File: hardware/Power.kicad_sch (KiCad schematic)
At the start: 70 parts, among them J10 I2C, J3 ESTOP, J4 PWR, J5 Conn_ARM_JTAG_SWD_10, J7 FAN, J9 DEBUG, Q1 MMBT5401LT1G, Q2 PSMN4R8-100BSEJ, Q3 MMBT3904, Q5 PSMN4R8-100BSEJ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

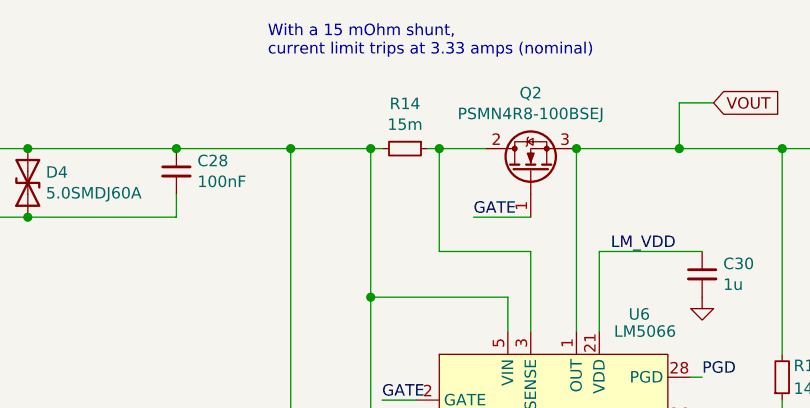
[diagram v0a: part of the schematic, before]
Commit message: Rsns to 5m (13A limit)
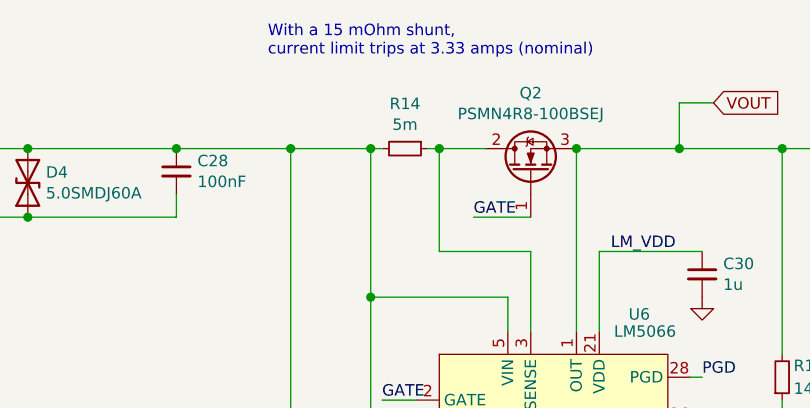
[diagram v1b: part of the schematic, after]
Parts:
- R14: value 15m -> 5m; D1PN WSLH-.015CT-ND -> 696-1182-2-ND; MFN Vishay Dale -> Riedon; MPN WSL2512R0150FEA18 -> CSR2512B0R005F
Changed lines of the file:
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@@
   (junction (at 259.08 97.79) (diameter 1.016) (color 0 0 0 0))
   (junction (at 259.08 105.41) (diameter 1.016) (color 0 0 0 0))
+  (no_connect (at 120.65 78.74))
+  (no_connect (at 120.65 81.28))
+  (no_connect (at 177.8 45.72))
+  (no_connect (at 198.12 55.88))
+  (no_connect (at 177.8 55.88))
   (no_connect (at 120.65 76.2))
-  (no_connect (at 177.8 55.88))
   (no_connect (at 254 50.8))
-  (no_connect (at 120.65 81.28))
-  (no_connect (at 90.17 83.82))
-  (no_connect (at 177.8 45.72))
   (no_connect (at 120.65 73.66))
   (no_connect (at 255.27 100.33))
-  (no_connect (at 198.12 55.88))
-  (no_connect (at 120.65 78.74))
+  (no_connect (at 90.17 83.82))
   (wire (pts (xy 16.51 120.65) (xy 25.4 120.65))
     (stroke (width 0) (type solid) (color 0 0 0 0))
@@
     (in_bom yes) (on_board yes)
     (property "Reference" "R14" (id 0) (at 88.9 22.9616 90))
-    (property "Value" "15m" (id 1) (at 88.9 25.273 90))
+    (property "Value" "5m" (id 1) (at 88.9 25.273 90))
     (property "Footprint" "Resistor_SMD:R_2512_6332Metric" (id 2) (at 88.9 27.94 0)
       (effects (font (size 1.27 1.27)) hide)
@@
       (effects (font (size 1.27 1.27)) hide)
     )
-    (property "D1PN" "WSLH-.015CT-ND" (id 5) (at 88.9 27.94 90)
-      (effects (font (size 1.27 1.27)) hide)
-    )
-    (property "MFN" "Vishay Dale" (id 6) (at 88.9 27.94 90)
-      (effects (font (size 1.27 1.27)) hide)
-    )
-    (property "MPN" "WSL2512R0150FEA18" (id 7) (at 88.9 27.94 90)
-      (effects (font (size 1.27 1.27)) hide)
-    )
+    (property "D1PN" "696-1182-2-ND" (id 5) (at 88.9 27.94 90)
+      (effects (font (size 1.27 1.27)) hide)
+    )
+    (property "MFN" "Riedon" (id 6) (at 88.9 27.94 90)
+      (effects (font (size 1.27 1.27)) hide)
+    )
+    (property "MPN" "CSR2512B0R005F" (id 7) (at 88.9 27.94 90)
+      (effects (font (size 1.27 1.27)) hide)
+    )

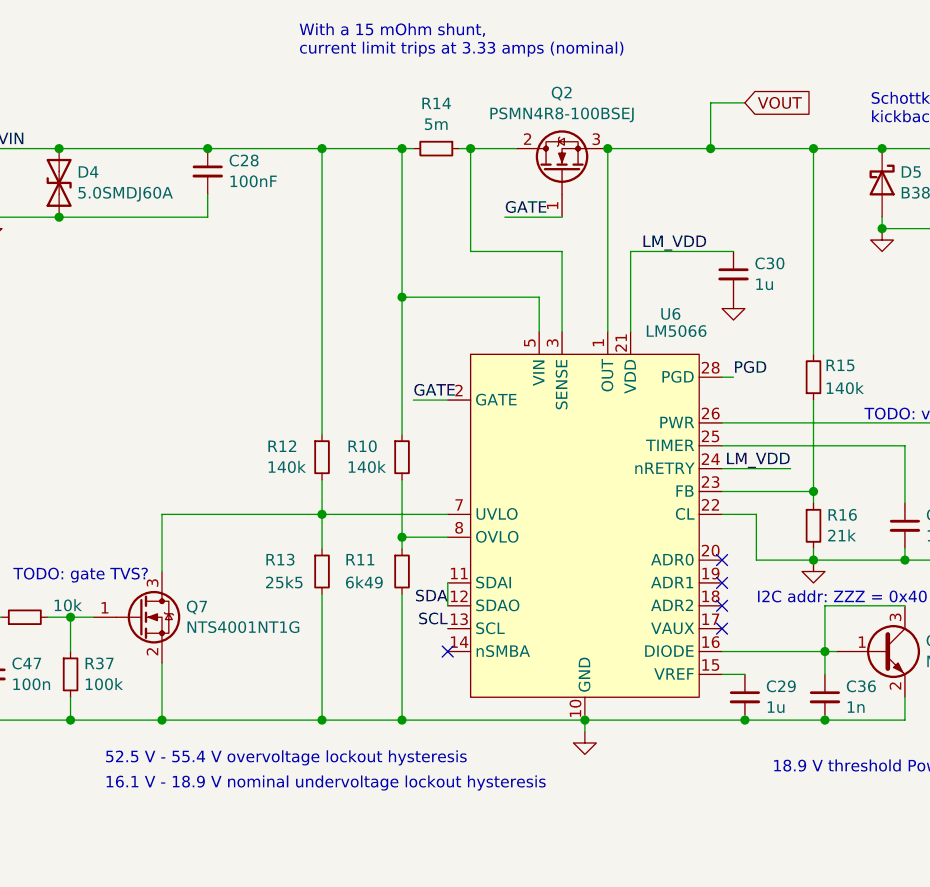
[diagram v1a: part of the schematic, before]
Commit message: Adding resistors for external divider (allows higher current sense)
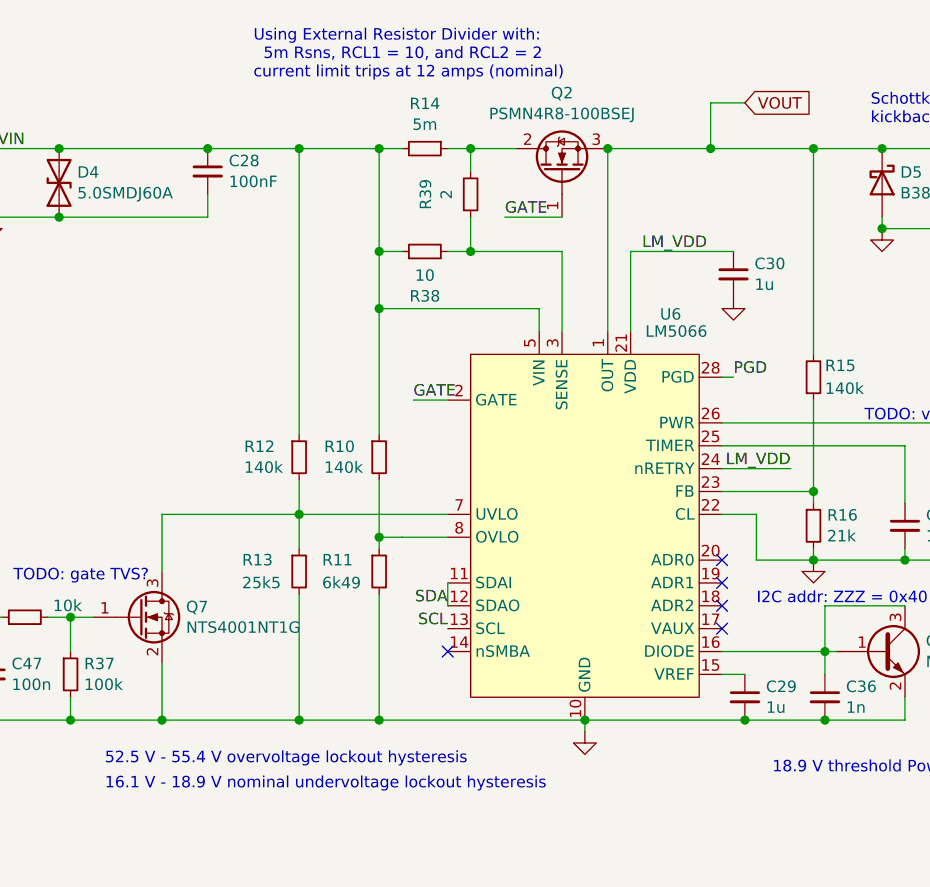
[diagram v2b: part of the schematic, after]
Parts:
- added R38: 10, Resistor_SMD:R_0603_1608Metric, symbol Device:R_Small
- added R39: 2, Resistor_SMD:R_0603_1608Metric, symbol Device:R_Small
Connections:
- net VIN: now also R38.1
- net at Q2.2 (D), R14.1: now also R39.2; no longer U6.3 (SENSE)
- new net: R38.2, R39.1, U6.3 (SENSE)
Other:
- note added: "Using External Resistor Divider with: 5m Rsns, RCL1 = 10, and RCL2 = 2 current limit trips at 12 amps (nominal)"
- note removed: "With a 15 mOhm shunt, current limit trips at 3.33 amps (nominal)"
- moved on the sheet: R10, R11, R12, R13, R14

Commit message: Adjusting timeout capacitor (1uF -> 52ms)
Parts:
- C31: value 100n -> 1u; D1PN 311-1344-1-ND -> 399-C0603C105K4RAC7411TR-ND; MFN Yageo -> KEMET; MPN CC0603KRX7R9BB104 -> C0603C105K4RAC7411
- R17: value 21k -> 300k; D1PN P21KDBCT-ND -> 311-300KHRTR-ND; MFN Panasonic -> Yageo; MPN ERA-3AEB2102V -> RC0603FR-07300KL
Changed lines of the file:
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@@
       (effects (font (size 1.27 1.27)) (justify left))
     )
-    (property "Value" "21k" (id 1) (at 151.3586 70.993 0)
+    (property "Value" "300k" (id 1) (at 151.3586 70.993 0)
       (effects (font (size 1.27 1.27)) (justify left))
     )
@@
       (effects (font (size 1.27 1.27)) hide)
     )
-    (property "D1PN" "P21KDBCT-ND" (id 5) (at 151.3586 66.1416 0)
-      (effects (font (size 1.27 1.27)) hide)
-    )
-    (property "MFN" "Panasonic" (id 6) (at 151.3586 66.1416 0)
-      (effects (font (size 1.27 1.27)) hide)
-    )
-    (property "MPN" "ERA-3AEB2102V" (id 7) (at 151.3586 66.1416 0)
+    (property "D1PN" "311-300KHRTR-ND" (id 5) (at 151.3586 66.1416 0)
+      (effects (font (size 1.27 1.27)) hide)
+    )
+    (property "MFN" "Yageo" (id 6) (at 151.3586 66.1416 0)
+      (effects (font (size 1.27 1.27)) hide)
+    )
+    (property "MPN" "RC0603FR-07300KL" (id 7) (at 151.3586 66.1416 0)
       (effects (font (size 1.27 1.27)) hide)
     )
@@
       (effects (font (size 1.27 1.27)) (justify left))
     )
-    (property "Value" "100n" (id 1) (at 143.3068 70.993 0)
+    (property "Value" "1u" (id 1) (at 143.3068 70.993 0)
       (effects (font (size 1.27 1.27)) (justify left))
     )
@@
       (effects (font (size 1.27 1.27)) hide)
     )
-    (property "D1PN" "311-1344-1-ND" (id 5) (at 143.3068 66.1416 0)
-      (effects (font (size 1.27 1.27)) hide)
-    )
-    (property "MFN" "Yageo" (id 6) (at 143.3068 66.1416 0)
-      (effects (font (size 1.27 1.27)) hide)
-    )
-    (property "MPN" "CC0603KRX7R9BB104" (id 7) (at 143.3068 66.1416 0)
-      (effects (font (size 1.27 1.27)) hide)
-    )
+    (property "D1PN" "399-C0603C105K4RAC7411TR-ND" (id 5) (at 143.3068 66.1416 0)
+      (effects (font (size 1.27 1.27)) hide)
+    )
+    (property "MFN" "KEMET" (id 6) (at 143.3068 66.1416 0)
+      (effects (font (size 1.27 1.27)) hide)
+    )
+    (property "MPN" "C0603C105K4RAC7411" (id 7) (at 143.3068 66.1416 0)
+      (effects (font (size 1.27 1.27)) hide)
+    )

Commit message: Adjusting feedback resistors.
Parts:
- R15: value 140k -> 240k; D1PN P140KDBCT-ND -> P240KDBTR-ND; MPN ERA-3AEB1403V -> ERA-3AEB244V
- R16: value 21k -> 13.3k; D1PN P21KDBCT-ND -> P13.3KDBTR-ND; MPN ERA-3AEB2102V -> ERA-3AEB1332V
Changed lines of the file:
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@@
       (effects (font (size 1.27 1.27)) (justify left))
     )
-    (property "Value" "140k" (id 1) (at 132.08 54.61 0)
+    (property "Value" "240k" (id 1) (at 132.08 54.61 0)
       (effects (font (size 1.27 1.27)) (justify left))
     )
@@
       (effects (font (size 1.27 1.27)) hide)
     )
-    (property "D1PN" "P140KDBCT-ND" (id 5) (at 132.08 54.61 0)
+    (property "D1PN" "P240KDBTR-ND" (id 5) (at 132.08 54.61 0)
       (effects (font (size 1.27 1.27)) hide)
     )
@@
       (effects (font (size 1.27 1.27)) hide)
     )
-    (property "MPN" "ERA-3AEB1403V" (id 7) (at 132.08 54.61 0)
+    (property "MPN" "ERA-3AEB244V" (id 7) (at 132.08 54.61 0)
       (effects (font (size 1.27 1.27)) hide)
     )
@@
       (effects (font (size 1.27 1.27)) (justify left))
     )
-    (property "Value" "21k" (id 1) (at 132.3086 70.993 0)
+    (property "Value" "13.3k" (id 1) (at 132.3086 70.993 0)
       (effects (font (size 1.27 1.27)) (justify left))
     )
@@
       (effects (font (size 1.27 1.27)) hide)
     )
-    (property "D1PN" "P21KDBCT-ND" (id 5) (at 132.3086 66.1416 0)
+    (property "D1PN" "P13.3KDBTR-ND" (id 5) (at 132.3086 66.1416 0)
       (effects (font (size 1.27 1.27)) hide)
     )
@@
       (effects (font (size 1.27 1.27)) hide)
     )
-    (property "MPN" "ERA-3AEB2102V" (id 7) (at 132.3086 66.1416 0)
+    (property "MPN" "ERA-3AEB1332V" (id 7) (at 132.3086 66.1416 0)
       (effects (font (size 1.27 1.27)) hide)
     )

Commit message: Revert "Adjusting timeout capacitor (1uF -> 52ms)"
This reverts commit 7a30909a9925d87866bd3a766fa9658db1f002d2.
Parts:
- C31: value 1u -> 100n; D1PN 399-C0603C105K4RAC7411TR-ND -> 311-1344-1-ND; MFN KEMET -> Yageo; MPN C0603C105K4RAC7411 -> CC0603KRX7R9BB104
- R17: value 300k -> 21k; D1PN 311-300KHRTR-ND -> P21KDBCT-ND; MFN Yageo -> Panasonic; MPN RC0603FR-07300KL -> ERA-3AEB2102V
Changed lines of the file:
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@@
       (effects (font (size 1.27 1.27)) (justify left))
     )
-    (property "Value" "300k" (id 1) (at 151.3586 70.993 0)
+    (property "Value" "21k" (id 1) (at 151.3586 70.993 0)
       (effects (font (size 1.27 1.27)) (justify left))
     )
@@
       (effects (font (size 1.27 1.27)) hide)
     )
-    (property "D1PN" "311-300KHRTR-ND" (id 5) (at 151.3586 66.1416 0)
-      (effects (font (size 1.27 1.27)) hide)
-    )
-    (property "MFN" "Yageo" (id 6) (at 151.3586 66.1416 0)
-      (effects (font (size 1.27 1.27)) hide)
-    )
-    (property "MPN" "RC0603FR-07300KL" (id 7) (at 151.3586 66.1416 0)
+    (property "D1PN" "P21KDBCT-ND" (id 5) (at 151.3586 66.1416 0)
+      (effects (font (size 1.27 1.27)) hide)
+    )
+    (property "MFN" "Panasonic" (id 6) (at 151.3586 66.1416 0)
+      (effects (font (size 1.27 1.27)) hide)
+    )
+    (property "MPN" "ERA-3AEB2102V" (id 7) (at 151.3586 66.1416 0)
       (effects (font (size 1.27 1.27)) hide)
     )
@@
       (effects (font (size 1.27 1.27)) (justify left))
     )
-    (property "Value" "1u" (id 1) (at 143.3068 70.993 0)
+    (property "Value" "100n" (id 1) (at 143.3068 70.993 0)
       (effects (font (size 1.27 1.27)) (justify left))
     )
@@
       (effects (font (size 1.27 1.27)) hide)
     )
-    (property "D1PN" "399-C0603C105K4RAC7411TR-ND" (id 5) (at 143.3068 66.1416 0)
-      (effects (font (size 1.27 1.27)) hide)
-    )
-    (property "MFN" "KEMET" (id 6) (at 143.3068 66.1416 0)
-      (effects (font (size 1.27 1.27)) hide)
-    )
-    (property "MPN" "C0603C105K4RAC7411" (id 7) (at 143.3068 66.1416 0)
-      (effects (font (size 1.27 1.27)) hide)
-    )
+    (property "D1PN" "311-1344-1-ND" (id 5) (at 143.3068 66.1416 0)
+      (effects (font (size 1.27 1.27)) hide)
+    )
+    (property "MFN" "Yageo" (id 6) (at 143.3068 66.1416 0)
+      (effects (font (size 1.27 1.27)) hide)
+    )
+    (property "MPN" "CC0603KRX7R9BB104" (id 7) (at 143.3068 66.1416 0)
+      (effects (font (size 1.27 1.27)) hide)
+    )

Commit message: Bumping Rpwr
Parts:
- removed R38: 10, Resistor_SMD:R_0603_1608Metric, symbol Device:R_Small
- removed R39: 2, Resistor_SMD:R_0603_1608Metric, symbol Device:R_Small
- R14: value 5m -> 4m; D1PN 696-1182-2-ND -> WSLH-.004TR-ND; MFN Riedon -> Vishay Dale; MPN CSR2512B0R005F -> WSL25124L000FEA18
- R17: value 21k -> 300k; D1PN P21KDBCT-ND -> P300KDBTR-ND; MPN ERA-3AEB2102V -> ERA-3AEB304V
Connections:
- net at Q2.2 (D), R14.1: now also U6.3 (SENSE)
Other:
- note added: "Using 4m Rsns, current limit trips at 12.5 amps (nominal)"
- note removed: "Using External Resistor Divider with: 5m Rsns, RCL1 = 10, and RCL2 = 2 current limit trips at 12 amps (nominal)"
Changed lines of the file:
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@@
   (junction (at 78.74 139.7) (diameter 1.016) (color 0 0 0 0))
   (junction (at 82.55 27.94) (diameter 1.016) (color 0 0 0 0))
-  (junction (at 82.55 39.37) (diameter 1.016) (color 0 0 0 0))
   (junction (at 82.55 45.72) (diameter 1.016) (color 0 0 0 0))
   (junction (at 82.55 71.12) (diameter 1.016) (color 0 0 0 0))
   (junction (at 82.55 91.44) (diameter 1.016) (color 0 0 0 0))
   (junction (at 92.71 27.94) (diameter 1.016) (color 0 0 0 0))
-  (junction (at 92.71 39.37) (diameter 1.016) (color 0 0 0 0))
   (junction (at 105.41 91.44) (diameter 1.016) (color 0 0 0 0))
   (junction (at 107.95 27.94) (diameter 1.016) (color 0 0 0 0))
@@
   (junction (at 259.08 97.79) (diameter 1.016) (color 0 0 0 0))
   (junction (at 259.08 105.41) (diameter 1.016) (color 0 0 0 0))
+  (no_connect (at 254 50.8))
+  (no_connect (at 90.17 83.82))
+  (no_connect (at 255.27 100.33))
+  (no_connect (at 198.12 55.88))
+  (no_connect (at 120.65 73.66))
+  (no_connect (at 120.65 76.2))
+  (no_connect (at 120.65 81.28))
   (no_connect (at 120.65 78.74))
-  (no_connect (at 120.65 81.28))
+  (no_connect (at 177.8 55.88))
   (no_connect (at 177.8 45.72))
-  (no_connect (at 198.12 55.88))
-  (no_connect (at 177.8 55.88))
-  (no_connect (at 120.65 76.2))
-  (no_connect (at 254 50.8))
-  (no_connect (at 120.65 73.66))
-  (no_connect (at 255.27 100.33))
-  (no_connect (at 90.17 83.82))
   (wire (pts (xy 16.51 120.65) (xy 25.4 120.65))
     (stroke (width 0) (type solid) (color 0 0 0 0))
@@
     (stroke (width 0) (type solid) (color 0 0 0 0))
   )
-  (wire (pts (xy 82.55 27.94) (xy 82.55 39.37))
+  (wire (pts (xy 82.55 27.94) (xy 82.55 45.72))
     (stroke (width 0) (type solid) (color 0 0 0 0))
   )
@@
     (stroke (width 0) (type solid) (color 0 0 0 0))
   )
-  (wire (pts (xy 82.55 39.37) (xy 82.55 45.72))
-    (stroke (width 0) (type solid) (color 0 0 0 0))
-  )
-  (wire (pts (xy 82.55 39.37) (xy 85.09 39.37))
-    (stroke (width 0) (type solid) (color 0 0 0 0))
-  )
   (wire (pts (xy 82.55 45.72) (xy 82.55 59.69))
     (stroke (width 0) (type solid) (color 0 0 0 0))
@@
     (stroke (width 0) (type solid) (color 0 0 0 0))
   )
-  (wire (pts (xy 82.55 71.12) (xy 85.09 71.12))
+  (wire (pts (xy 82.55 71.12) (xy 90.17 71.12))
     (stroke (width 0) (type solid) (color 0 0 0 0))
   )
@@
     (stroke (width 0) (type solid) (color 0 0 0 0))
   )
-  (wire (pts (xy 85.09 71.12) (xy 90.17 71.12))
-    (stroke (width 0) (type solid) (color 0 0 0 0))
-  )
   (wire (pts (xy 86.36 55.88) (xy 90.17 55.88))
     (stroke (width 0) (type solid) (color 0 0 0 0))
@@
     (stroke (width 0) (type solid) (color 0 0 0 0))
   )
-  (wire (pts (xy 90.17 39.37) (xy 92.71 39.37))
-    (stroke (width 0) (type solid) (color 0 0 0 0))
-  )
   (wire (pts (xy 90.17 76.2) (xy 90.17 78.74))
     (stroke (width 0) (type solid) (color 0 0 0 0))
@@
     (stroke (width 0) (type solid) (color 0 0 0 0))
   )
-  (wire (pts (xy 92.71 35.56) (xy 92.71 39.37))
+  (wire (pts (xy 92.71 30.48) (xy 92.71 39.37))
     (stroke (width 0) (type solid) (color 0 0 0 0))
   )
@@
     (effects (font (size 1.27 1.27)) (justify left bottom))
   )
-  (text "Using External Resistor Divider with:\n  5m Rsns, RCL1 = 10, and RCL2 = 2\ncurrent limit trips at 12 amps (nominal)"
+  (text "Using 4m Rsns,\ncurrent limit trips at 12.5 amps (nominal)"
     (at 68.58 20.32 0)
     (effects (font (size 1.27 1.27)) (justify left bottom))
@@
     (in_bom yes) (on_board yes)
     (property "Reference" "R14" (id 0) (at 87.63 22.9616 90))
-    (property "Value" "5m" (id 1) (at 87.63 25.273 90))
+    (property "Value" "4m" (id 1) (at 87.63 25.273 90))
     (property "Footprint" "Resistor_SMD:R_2512_6332Metric" (id 2) (at 87.63 27.94 0)
       (effects (font (size 1.27 1.27)) hide)
@@
       (effects (font (size 1.27 1.27)) hide)
     )
-    (property "D1PN" "696-1182-2-ND" (id 5) (at 87.63 27.94 90)
-      (effects (font (size 1.27 1.27)) hide)
-    )
-    (property "MFN" "Riedon" (id 6) (at 87.63 27.94 90)
-      (effects (font (size 1.27 1.27)) hide)
-    )
-    (property "MPN" "CSR2512B0R005F" (id 7) (at 87.63 27.94 90)
-      (effects (font (size 1.27 1.27)) hide)
-    )
-  )
-  (symbol (lib_id "Device:R_Small") (at 87.63 39.37 90) (unit 1)
-    (in_bom yes) (on_board yes)
-    (property "Reference" "R38" (id 0) (at 87.63 44.3484 90))
-    (property "Value" "10" (id 1) (at 87.63 42.037 90))
-    (property "Footprint" "Resistor_SMD:R_0603_1608Metric" (id 2) (at 87.63 39.37 0)
-      (effects (font (size 1.27 1.27)) hide)
-    )
-    (property "Datasheet" "" (id 3) (at 87.63 39.37 0)
-      (effects (font (size 1.27 1.27)) hide)
-    )
-    (property "D1N" "Digikey" (id 4) (at 87.63 39.37 90)
-      (effects (font (size 1.27 1.27)) hide)
-    )
-    (property "D1PN" "311-10.0HRTR-ND" (id 5) (at 87.63 39.37 90)
-      (effects (font (size 1.27 1.27)) hide)
-    )
-    (property "MFN" "Yageo" (id 6) (at 87.63 39.37 90)
-      (effects (font (size 1.27 1.27)) hide)
-    )
-    (property "MPN" "RC0603FR-0710RL" (id 7) (at 87.63 39.37 90)
-      (effects (font (size 1.27 1.27)) hide)
-    )
-  )
-  (symbol (lib_id "Device:R_Small") (at 92.71 33.02 0) (mirror x) (unit 1)
-    (in_bom yes) (on_board yes)
-    (property "Reference" "R39" (id 0) (at 87.7316 33.02 90))
-    (property "Value" "2" (id 1) (at 90.043 33.02 90))
-    (property "Footprint" "Resistor_SMD:R_0603_1608Metric" (id 2) (at 92.71 33.02 0)
-      (effects (font (size 1.27 1.27)) hide)
-    )
-    (property "Datasheet" "" (id 3) (at 92.71 33.02 0)
-      (effects (font (size 1.27 1.27)) hide)
-    )
-    (property "D1N" "Digikey" (id 4) (at 92.71 33.02 90)
-      (effects (font (size 1.27 1.27)) hide)
-    )
-    (property "D1PN" "311-2.00HRTR-ND" (id 5) (at 92.71 33.02 90)
-      (effects (font (size 1.27 1.27)) hide)
-    )
-    (property "MFN" "Yageo" (id 6) (at 92.71 33.02 90)
-      (effects (font (size 1.27 1.27)) hide)
-    )
-    (property "MPN" "RC0603FR-072RL" (id 7) (at 92.71 33.02 90)
+    (property "D1PN" "WSLH-.004TR-ND" (id 5) (at 87.63 27.94 90)
+      (effects (font (size 1.27 1.27)) hide)
+    )
+    (property "MFN" "Vishay Dale" (id 6) (at 87.63 27.94 90)
+      (effects (font (size 1.27 1.27)) hide)
+    )
+    (property "MPN" "WSL25124L000FEA18" (id 7) (at 87.63 27.94 90)
       (effects (font (size 1.27 1.27)) hide)
     )
@@
       (effects (font (size 1.27 1.27)) (justify left))
     )
-    (property "Value" "21k" (id 1) (at 151.3586 70.993 0)
+    (property "Value" "300k" (id 1) (at 151.3586 70.993 0)
       (effects (font (size 1.27 1.27)) (justify left))
     )
@@
       (effects (font (size 1.27 1.27)) hide)
     )
-    (property "D1PN" "P21KDBCT-ND" (id 5) (at 151.3586 66.1416 0)
+    (property "D1PN" "P300KDBTR-ND" (id 5) (at 151.3586 66.1416 0)
       (effects (font (size 1.27 1.27)) hide)
     )
@@
       (effects (font (size 1.27 1.27)) hide)
     )
-    (property "MPN" "ERA-3AEB2102V" (id 7) (at 151.3586 66.1416 0)
-      (effects (font (size 1.27 1.27)) hide)
-    )
+    (property "MPN" "ERA-3AEB304V" (id 7) (at 151.3586 66.1416 0)
+      (effects (font (size 1.27 1.27)) hide)
+    )
